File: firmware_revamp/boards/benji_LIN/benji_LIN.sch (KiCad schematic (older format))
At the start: 37 parts, among them J1 CONN_02X03, J2 Conn_01x11, J3 Conn_01x11, J4 CONN_01X03, J5 CONN_01x02, J6 CONN_01X03, SW1 SW_Push_SPST_NO, U1 MCP2561-E_SN, U2 ATMEGA16M1, U3 TLIN1021DRQ1, Y1 Crystal_SMD

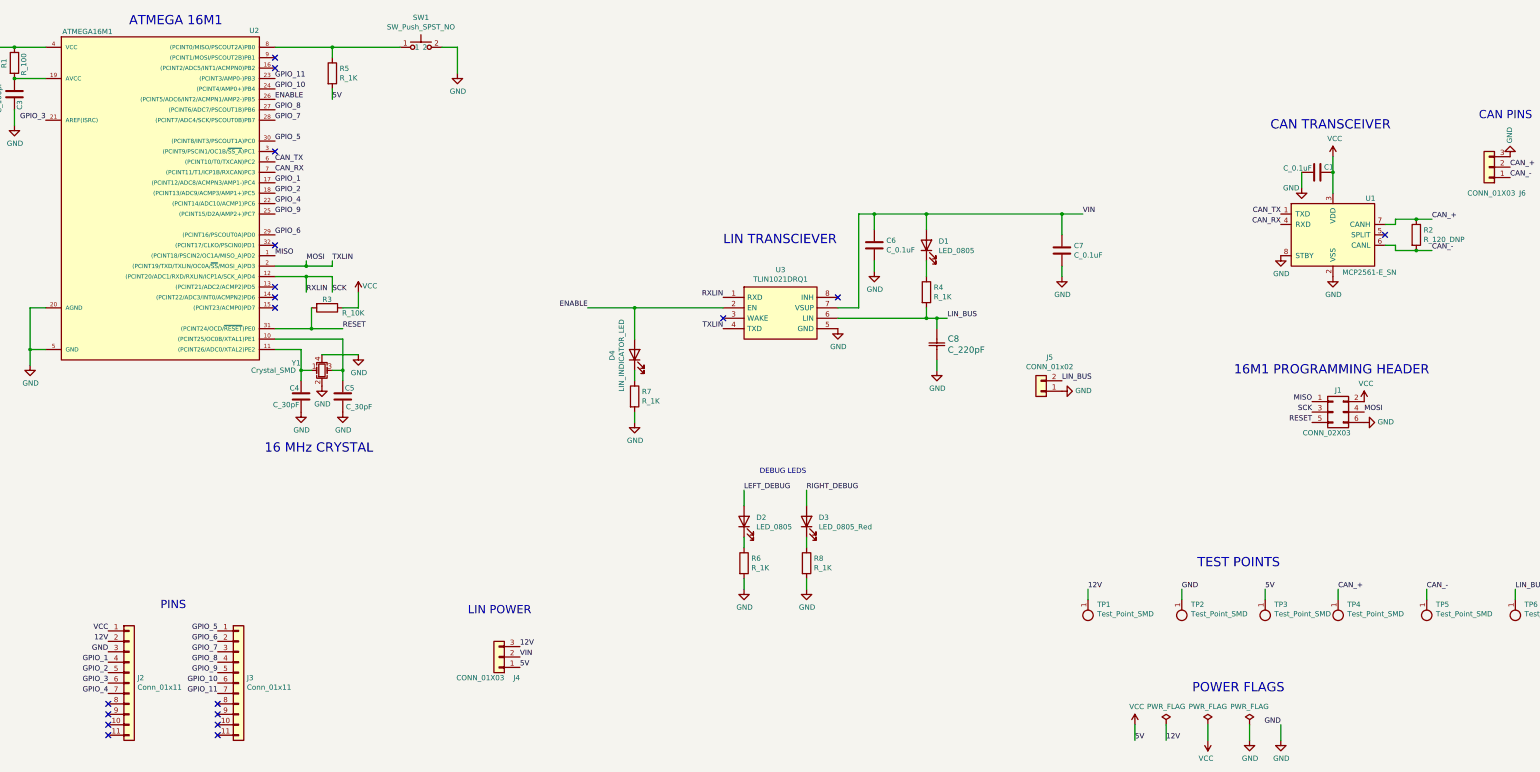
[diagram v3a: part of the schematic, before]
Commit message: Fixed vias, pins, rearranged debug lEDs
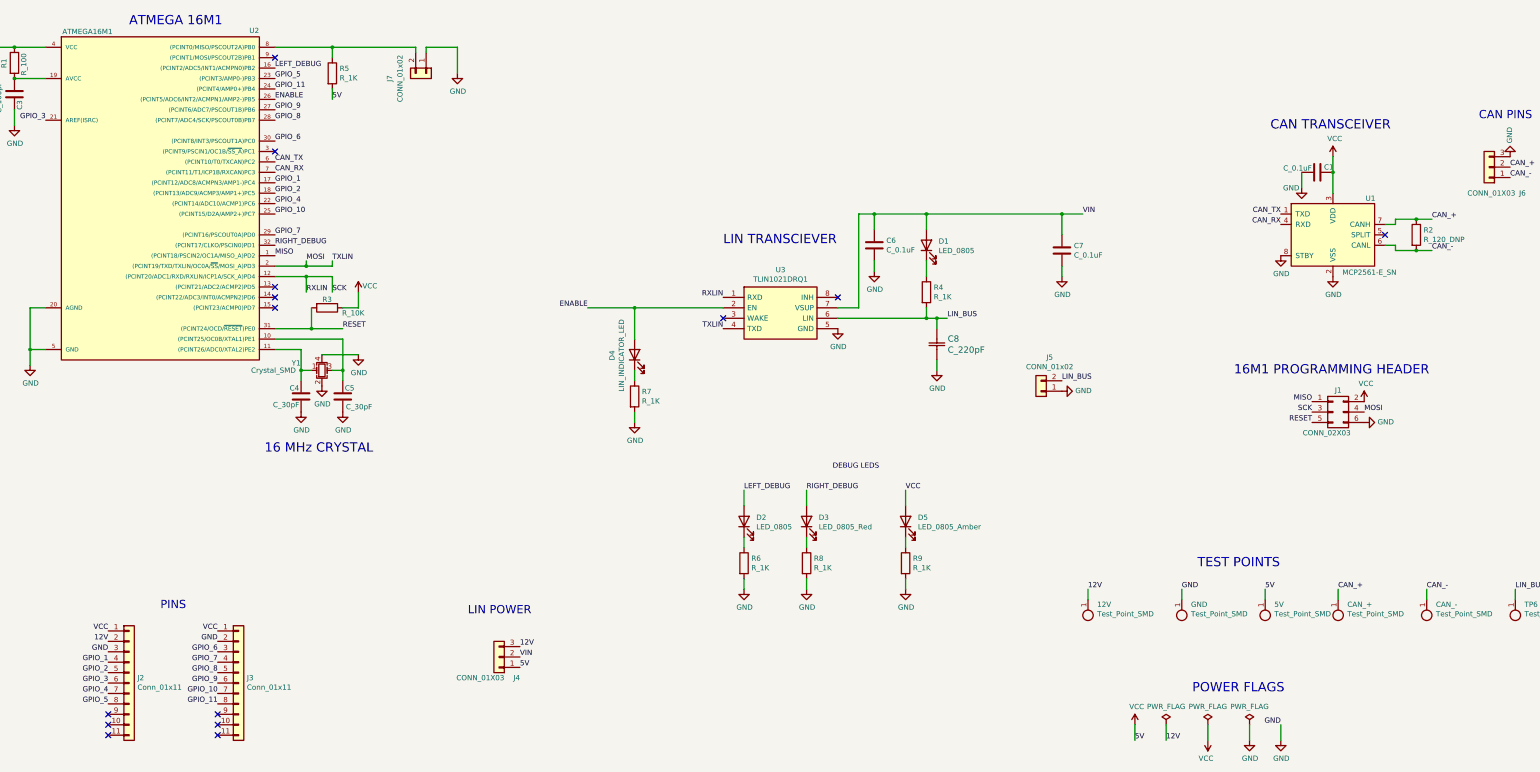
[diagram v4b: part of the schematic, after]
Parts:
- removed SW1: SW_Push_SPST_NO, footprints:SW_B3U-1000P_4.2x1.7mm, symbol formula:SW_Push_SPST_NO
- added D5: LED_0805_Amber, footprints:LED_0805_OEM, symbol formula:LED_0805_Amber
- added J7: CONN_01x02, Connector_PinHeader_2.54mm:PinHeader_1x02_P2.54mm_Vertical, symbol formula:CONN_01x02
- added R9: R_1K, footprints:R_0805_OEM, symbol formula:R_1K
- renumbered TP1 to 12V, TP3 to 5V, TP4 to CAN_+, TP5 to CAN_-, TP2 to GND
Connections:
- net GND: now also J3.2, J7.1 (Pin_1), R9.2
- net GPIO_10: now also J3.7, U2.25 ((PCINT15/D2A/AMP2+)PC7); no longer J3.6, U2.24 ((PCINT4/AMP0+)PB4)
- net GPIO_11: now also J3.8, U2.24 ((PCINT4/AMP0+)PB4); no longer J3.7, U2.23 ((PCINT3/AMP0-)PB3)
- net GPIO_5: now also J2.8, U2.23 ((PCINT3/AMP0-)PB3); no longer J3.1, U2.30 ((PCINT8/INT3/PSCOUT1A)PC0)
- net GPIO_6: now also J3.3, U2.30 ((PCINT8/INT3/PSCOUT1A)PC0); no longer J3.2, U2.29 ((PCINT16/PSCOUT0A)PD0)
- net GPIO_7: now also J3.4, U2.29 ((PCINT16/PSCOUT0A)PD0); no longer J3.3, U2.28 ((PCINT7/ADC4/SCK/PSCOUT0B)PB7)
- net GPIO_8: now also J3.5, U2.28 ((PCINT7/ADC4/SCK/PSCOUT0B)PB7); no longer J3.4, U2.27 ((PCINT6/ADC7/PSCOUT1B)PB6)
- net GPIO_9: now also J3.6, U2.27 ((PCINT6/ADC7/PSCOUT1B)PB6); no longer J3.5, U2.25 ((PCINT15/D2A/AMP2+)PC7)
- net LEFT_DEBUG: now also U2.16 ((PCINT2/ADC5/INT1/ACMPN0)PB2)
- net RIGHT_DEBUG: now also U2.32 ((PCINT17/CLKO/PSCIN0)PD1)
- net VCC: now also J3.1, D5.2 (A)
- net at R5.1, U2.8 ((PCINT0/MISO/PSCOUT2A)PB0): now also J7.2 (Pin_2)
- new net: D5.1 (K), R9.1
- no-connect marks 18 -> 14
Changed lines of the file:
@@
 Text Label 15550 6200 0    50   ~ 0
 LIN_BUS
-Text Notes 8300 5100 0    50   ~ 0
+Text Notes 9000 5050 0    50   ~ 0
 DEBUG LEDS
 $Comp
@@
 ENABLE
 NoConn ~ 3650 1100
-NoConn ~ 3650 1200
 NoConn ~ 3650 2000
-NoConn ~ 3650 2900
 Text Label 3650 3000 0    50   ~ 0
 MISO
@@
 Wire Wire Line
 	4200 1100 4200 1000
-Wire Wire Line
-	5400 1000 5250 1000
-$Comp
-L formula:SW_Push_SPST_NO SW1
-U 1 1 603700F1
-P 5050 1000
-F 0 "SW1" H 5050 1285 50  0000 C CNN
-F 1 "SW_Push_SPST_NO" H 5050 1194 50  0000 C CNN
-F 2 "footprints:SW_B3U-1000P_4.2x1.7mm" H 5050 1050 50  0001 C CNN
-F 3 "https://omronfs.omron.com/en_US/ecb/products/pdf/en-b3u.pdf" H 5050 1050 50  0001 C CNN
-F 4 "DK" H 5350 1350 50  0001 C CNN "MFN"
-F 5 "SW1020CT-ND" H 5250 1250 50  0001 C CNN "MPN"
-F 6 "https://www.digikey.com/product-detail/en/omron-electronics-inc-emc-div/B3U-1000P/SW1020CT-ND/1534357A" H 5450 1450 50  0001 C CNN "PurchasingLink"
-	1    5050 1000
-	1    0    0    -1
-$EndComp
 Wire Wire Line
 	3650 1000 4200 1000
@@
 $EndComp
 $Comp
-L formula:Test_Point_SMD TP1
+L formula:Test_Point_SMD 12V
 U 1 1 603FFDF1
 P 11450 6350
-F 0 "TP1" H 11362 6346 50  0000 R CNN
+F 0 "12V" H 11362 6346 50  0000 R CNN
 F 1 "Test_Point_SMD" H 11362 6437 50  0000 R CNN
 F 2 "footprints:Test_Point_SMD" H 11450 6200 50  0001 C CNN
@@
 $EndComp
 $Comp
-L formula:Test_Point_SMD TP2
+L formula:Test_Point_SMD GND
 U 1 1 60414A2B
 P 12350 6350
-F 0 "TP2" H 12262 6346 50  0000 R CNN
+F 0 "GND" H 12262 6346 50  0000 R CNN
 F 1 "Test_Point_SMD" H 12262 6437 50  0000 R CNN
 F 2 "footprints:Test_Point_SMD" H 12350 6200 50  0001 C CNN
@@
 $EndComp
 $Comp
-L formula:Test_Point_SMD TP3
+L formula:Test_Point_SMD 5V
 U 1 1 60414DEF
 P 13150 6350
-F 0 "TP3" H 13062 6346 50  0000 R CNN
+F 0 "5V" H 13062 6346 50  0000 R CNN
 F 1 "Test_Point_SMD" H 13062 6437 50  0000 R CNN
 F 2 "footprints:Test_Point_SMD" H 13150 6200 50  0001 C CNN
@@
 $EndComp
 $Comp
-L formula:Test_Point_SMD TP4
+L formula:Test_Point_SMD CAN_+
 U 1 1 60415519
 P 13850 6350
-F 0 "TP4" H 13762 6346 50  0000 R CNN
+F 0 "CAN_+" H 13762 6346 50  0000 R CNN
 F 1 "Test_Point_SMD" H 13762 6437 50  0000 R CNN
 F 2 "footprints:Test_Point_SMD" H 13850 6200 50  0001 C CNN
@@
 $EndComp
 $Comp
-L formula:Test_Point_SMD TP5
+L formula:Test_Point_SMD CAN_-
 U 1 1 604158E2
 P 14700 6350
-F 0 "TP5" H 14612 6346 50  0000 R CNN
+F 0 "CAN_-" H 14612 6346 50  0000 R CNN
 F 1 "Test_Point_SMD" H 14612 6437 50  0000 R CNN
 F 2 "footprints:Test_Point_SMD" H 14700 6200 50  0001 C CNN
@@
 Text Label 2050 6800 2    50   ~ 0
 GND
-NoConn ~ 3100 7300
 NoConn ~ 3100 7400
 NoConn ~ 3100 7500
@@
 NoConn ~ 2050 7500
 NoConn ~ 2050 7400
-NoConn ~ 2050 7300
 Connection ~ 4200 1000
 Wire Wire Line
 	5400 1000 5400 1250
-Wire Wire Line
-	4200 1000 4850 1000
 Text Label 6000 6850 0    50   ~ 0
 VIN
@@
 GPIO_4
 Text Label 3650 1300 0    50   ~ 0
+GPIO_5
+Text Label 3650 1400 0    50   ~ 0
 GPIO_11
-Text Label 3650 1400 0    50   ~ 0
-GPIO_10
 Text Label 3650 2300 0    50   ~ 0
 GPIO_1
@@
 GPIO_2
 Text Label 3650 1900 0    50   ~ 0
-GPIO_5
+GPIO_6
 Text Label 3650 2800 0    50   ~ 0
-GPIO_6
+GPIO_7
 Text Label 3650 1700 0    50   ~ 0
-GPIO_7
+GPIO_8
 Text Label 3650 1600 0    50   ~ 0
-GPIO_8
+GPIO_9
 Text Label 3650 2600 0    50   ~ 0
-GPIO_9
+GPIO_10
 $Comp
 L formula:Conn_01x11 J2
@@
 Text Label 2050 7200 2    50   ~ 0
 GPIO_4
+Text Label 2050 7300 2    50   ~ 0
+GPIO_5
+Text Label 3100 6800 2    50   ~ 0
+GPIO_6
+Text Label 3100 6900 2    50   ~ 0
+GPIO_7
+Text Label 3100 7000 2    50   ~ 0
+GPIO_8
+Text Label 3100 7100 2    50   ~ 0
+GPIO_9
+Text Label 3100 7200 2    50   ~ 0
+GPIO_10
+Text Label 3100 7300 2    50   ~ 0
+GPIO_11
+$Comp
+L formula:LED_0805_Amber D5
+U 1 1 606678A5
+P 9700 5550
+F 0 "D5" V 9739 5432 50  0000 R CNN
+F 1 "LED_0805_Amber" V 9648 5432 50  0000 R CNN
+F 2 "footprints:LED_0805_OEM" H 9600 5550 50  0001 C CNN
+F 3 "https://media.digikey.com/pdf/Data%20Sheets/Chicago%20Miniature%20Lamps%20PDFs/CMDA5_Series_Rev_Aug_2014.pdf" H 9700 5650 50  0001 C CNN
+F 4 "DK" H 9700 5550 60  0001 C CNN "MFN"
+F 5 "L71517CT-ND" H 9700 5550 60  0001 C CNN "MPN"
+F 6 "https://www.digikey.com/product-detail/en/visual-communications-company-vcc/CMDA5DY7D1S/L71517CT-ND/614867" H 10100 6050 60  0001 C CNN "PurchasingLink"
+	1    9700 5550
+	0    -1   -1   0
+$EndComp
+Text Label 9700 5250 0    50   ~ 0
+VCC
+Wire Wire Line
+	9700 5250 9700 5400
+$Comp
+L formula:R_1K R9
+U 1 1 6066FCA6
+P 9700 5950
+F 0 "R9" H 9770 5996 50  0000 L CNN
+F 1 "R_1K" H 9770 5905 50  0000 L CNN
+F 2 "footprints:R_0805_OEM" H 9630 5950 50  0001 C CNN
+F 3 "https://www.seielect.com/Catalog/SEI-rncp.pdf" H 9780 5950 50  0001 C CNN
+F 4 "DK" H 9700 5950 60  0001 C CNN "MFN"
+F 5 "RNCP0805FTD1K00CT-ND" H 9700 5950 60  0001 C CNN "MPN"
+F 6 "https://www.digikey.com/products/en?keywords=RNCP0805FTD1K00CT-ND" H 10180 6350 60  0001 C CNN "PurchasingLink"
+	1    9700 5950
+	1    0    0    -1
+$EndComp
+Wire Wire Line
+	9700 5800 9700 5700
+$Comp
+L power:GND #PWR024
+U 1 1 606730CC
+P 9700 6200
+F 0 "#PWR024" H 9700 5950 50  0001 C CNN
+F 1 "GND" H 9705 6027 50  0000 C CNN
+F 2 "" H 9700 6200 50  0001 C CNN
+F 3 "" H 9700 6200 50  0001 C CNN
+	1    9700 6200
+	1    0    0    -1
+$EndComp
+Wire Wire Line
+	9700 6200 9700 6100
+Text Label 3100 6700 2    50   ~ 0
+GND
 Text Label 3100 6600 2    50   ~ 0
-GPIO_5
-Text Label 3100 6700 2    50   ~ 0
-GPIO_6
-Text Label 3100 6800 2    50   ~ 0
-GPIO_7
-Text Label 3100 6900 2    50   ~ 0
-GPIO_8
-Text Label 3100 7000 2    50   ~ 0
-GPIO_9
-Text Label 3100 7100 2    50   ~ 0
-GPIO_10
-Text Label 3100 7200 2    50   ~ 0
-GPIO_11
+VCC
+$Comp
+L formula:CONN_01x02 J7
+U 1 1 60655BBB
+P 5100 1250
+F 0 "J7" H 5150 900 50  0000 C CNN
+F 1 "CONN_01x02" H 5150 1000 50  0000 C CNN
+F 2 "Connector_PinHeader_2.54mm:PinHeader_1x02_P2.54mm_Vertical" H 5000 1250 50  0001 C CNN
+F 3 "https://katalog.we-online.de/em/datasheet/6130xx11121.pdf" H 5100 1350 50  0001 C CNN
+F 4 "DK" H 5200 1450 50  0001 C CNN "MFN"
+F 5 "732-5315-ND" H 5300 1550 50  0001 C CNN "MPN"
+	1    5100 1250
+	0    1    1    0
+$EndComp
+Wire Wire Line
+	5000 1000 5000 1050
+Wire Wire Line
+	4200 1000 5000 1000
+Wire Wire Line
+	5100 1000 5100 1050
+Wire Wire Line
+	5100 1000 5400 1000
+Text Label 3650 2900 0    50   ~ 0
+RIGHT_DEBUG
+Text Label 3650 1200 0    50   ~ 0
+LEFT_DEBUG
 $EndSCHEMATC

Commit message: Rearranged mostly visual errors, removed diode
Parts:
- removed D1: LED_0805, footprints:LED_0805_OEM, symbol formula:LED_0805
- removed GND: Test_Point_SMD, footprints:Test_Point_SMD, symbol formula:Test_Point_SMD
- renumbered 12V to 12V1, 5V to 5V1, CAN_+ to CAN_+1, CAN_- to CAN_-1
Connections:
- net ENABLE: now also U2.9 ((PCINT1/MOSI/PSCOUT2B)PB1); no longer U2.26 ((PCINT5/ADC6/INT2/ACMPN1/AMP2-)PB5)
- net GND: now also J3.1; no longer J3.2
- net LEFT_DEBUG: now also U2.13 ((PCINT21/ADC2/ACMP2)PD5); no longer U2.16 ((PCINT2/ADC5/INT1/ACMPN0)PB2)
- net RIGHT_DEBUG: now also U2.14 ((PCINT22/ADC3/INT0/ACMPN2)PD6); no longer U2.32 ((PCINT17/CLKO/PSCIN0)PD1)
- net VCC: no longer J3.1
- net VIN: now also R4.1
- net PD7: now reaches U2.15 ((PCINT23/ACMP0)PD7)
- net PD7: now also J2.4
- net PB4: now reaches J2.9
- net PB4: now also U2.24 ((PCINT4/AMP0+)PB4)
- net PC5: now reaches J3.9
- net PC5: now also U2.18 ((PCINT13/ADC9/ACMP3/AMP1+)PC5)
- net GPIO_1 renamed PC4
- net PC4: now also J2.6; no longer J2.4
- net GPIO_10 renamed PC7
- net GPIO_11 renamed PD1
- net PD1: now also U2.32 ((PCINT17/CLKO/PSCIN0)PD1); no longer U2.24 ((PCINT4/AMP0+)PB4)
- net GPIO_2 renamed PB2
- net PB2: now also U2.16 ((PCINT2/ADC5/INT1/ACMPN0)PB2); no longer U2.18 ((PCINT13/ADC9/ACMP3/AMP1+)PC5)
- net GPIO_3: no longer names the net of U2.21 (AREF(ISRC))
- net GPIO_3: no longer J2.6
- net GPIO_4 renamed PC6
- net GPIO_5 renamed PB3
- net GPIO_6 renamed PC0
- net PC0: now also J3.2; no longer J3.3
- net GPIO_7 renamed PB7
- net PB7: now also U2.28 ((PCINT7/ADC4/SCK/PSCOUT0B)PB7); no longer U2.29 ((PCINT16/PSCOUT0A)PD0)
- net GPIO_8 renamed PB6
- net PB6: now also U2.27 ((PCINT6/ADC7/PSCOUT1B)PB6); no longer U2.28 ((PCINT7/ADC4/SCK/PSCOUT0B)PB7)
- net GPIO_9 renamed PB5
- net PB5: now also U2.26 ((PCINT5/ADC6/INT2/ACMPN1/AMP2-)PB5); no longer U2.27 ((PCINT6/ADC7/PSCOUT1B)PB6)
- new net PD0: J3.3, U2.29 ((PCINT16/PSCOUT0A)PD0)
- no-connect marks 14 -> 9
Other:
- moved on the sheet: R3, R4

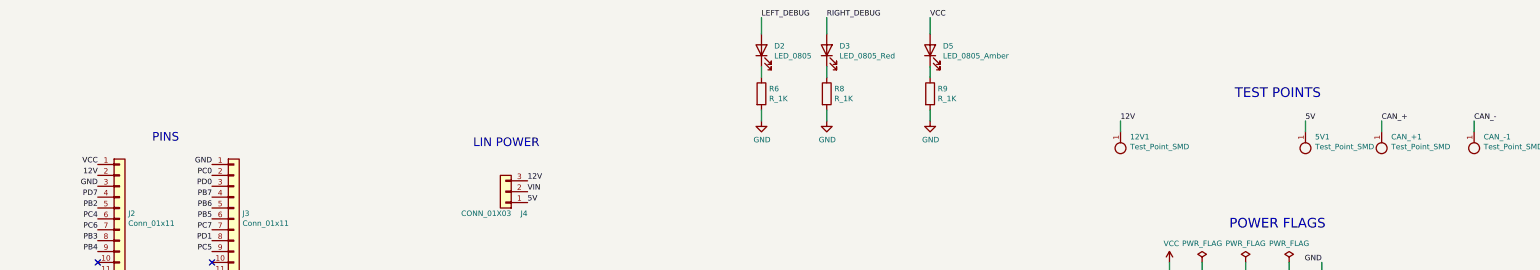
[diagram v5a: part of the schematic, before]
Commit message: Add labels to headers
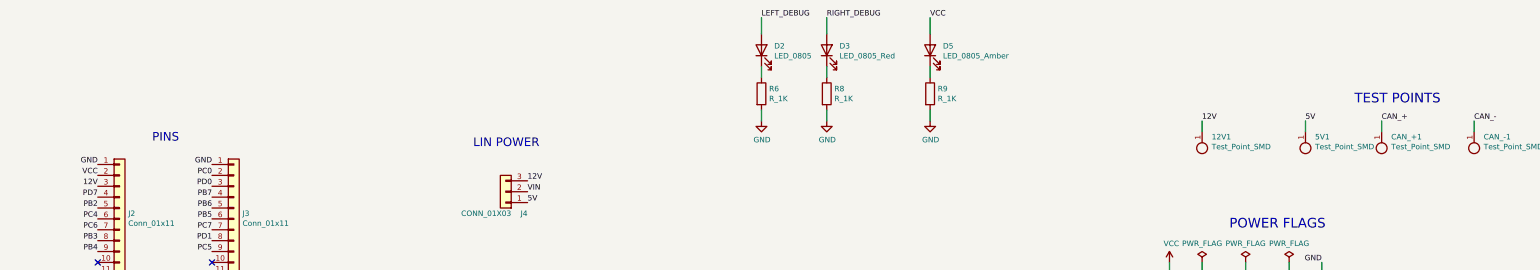
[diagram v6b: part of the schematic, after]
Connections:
- net 12V: now also J2.3; no longer J2.2
- net GND: now also J2.1; no longer J2.3
- net VCC: now also J2.2; no longer J2.1
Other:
- moved on the sheet: 12V1
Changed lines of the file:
@@
 Wire Wire Line
 	15550 6300 15550 6200
-Text Notes 12500 6000 0    89   ~ 0
+Text Notes 13600 6050 0    89   ~ 0
 TEST POINTS
 Wire Wire Line
-	11450 6200 11450 6300
-Text Label 11450 6200 0    50   ~ 0
+	12200 6200 12200 6300
+Text Label 12200 6200 0    50   ~ 0
 12V
 Text Label 7950 3400 2    50   ~ 0
@@
 L formula:Test_Point_SMD 12V1
 U 1 1 603FFDF1
-P 11450 6350
-F 0 "12V1" H 11362 6346 50  0000 R CNN
-F 1 "Test_Point_SMD" H 11362 6437 50  0000 R CNN
-F 2 "footprints:Test_Point_SMD" H 11450 6200 50  0001 C CNN
-F 3 "" H 11450 6350 50  0001 C CNN
-	1    11450 6350
+P 12200 6350
+F 0 "12V1" H 12112 6346 50  0000 R CNN
+F 1 "Test_Point_SMD" H 12112 6437 50  0000 R CNN
+F 2 "footprints:Test_Point_SMD" H 12200 6200 50  0001 C CNN
+F 3 "" H 12200 6350 50  0001 C CNN
+	1    12200 6350
 	-1   0    0    1
 $EndComp
@@
 ENABLE
 Text Label 2050 6600 2    50   ~ 0
-VCC
-Text Label 2050 6800 2    50   ~ 0
 GND
 NoConn ~ 3100 7500
@@
 	0    -1   -1   0
 $EndComp
-Text Label 2050 6700 2    50   ~ 0
-12V
 Wire Wire Line
 	1150 1600 1150 1750
@@
 Text Label 3100 6900 2    50   ~ 0
 PB7
+Text Label 2050 6800 2    50   ~ 0
+12V
+Text Label 2050 6700 2    50   ~ 0
+VCC
 $EndSCHEMATC

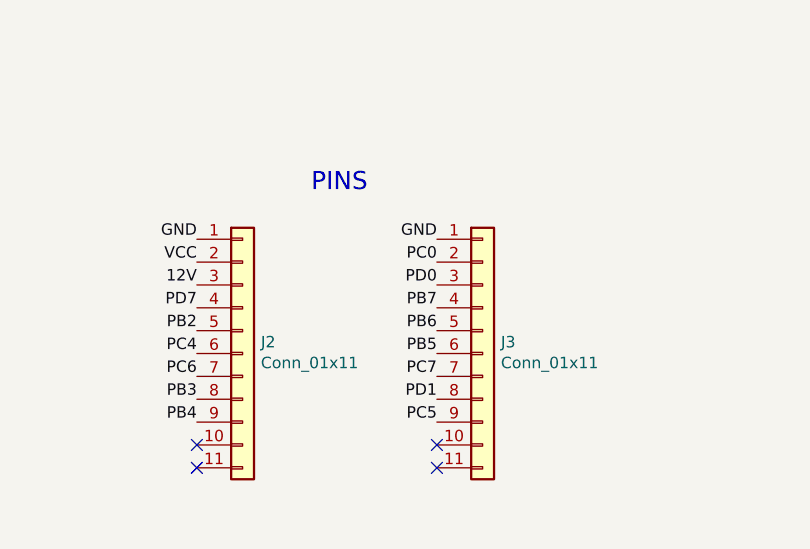
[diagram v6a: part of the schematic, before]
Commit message: Used correct headers, renamed pins where necessary
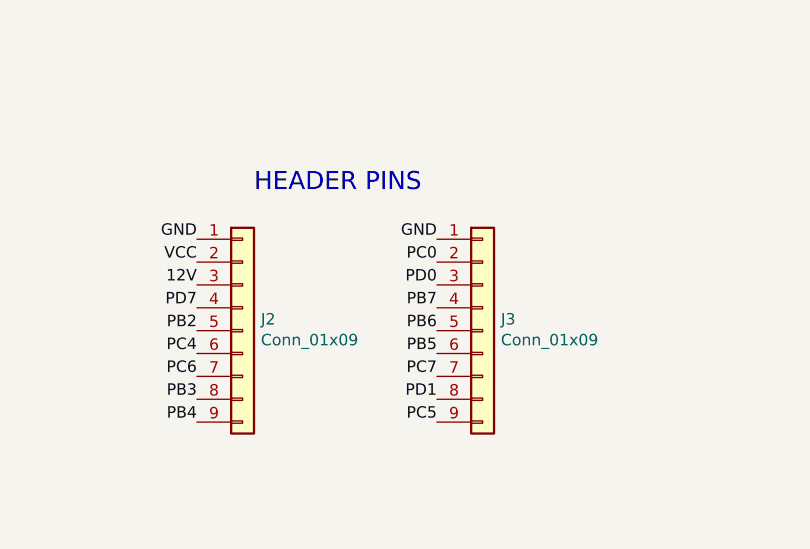
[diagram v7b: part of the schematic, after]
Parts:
- removed J2, J3: Conn_01x11, footprints:PinHeader_1x11_P2.54mm_Vertical, symbol formula:Conn_01x11
- added J2, J3: Conn_01x09, footprints:PinHeader_1x9_P2.54mm_Vertical, symbol formula:Conn_01x09
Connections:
- net 12V: now also J2.3
- net GND: now also J2.1, J3.1
- net PB2: now also J2.5
- net PB3: now also J2.8
- net PB4: now also J2.9
- net PB5: now also J3.6
- net PB6: now also J3.5
- net PB7: now also J3.4
- net PC0: now also J3.2
- net PC4: now also J2.6
- net PC5: now also J3.9
- net PC6: now also J2.7
- net PC7: now also J3.7
- net PD0: now also J3.3
- net PD1: now also J3.8
- net PD7: now also J2.4
- net VCC: now also J2.2
- no-connect marks 9 -> 5
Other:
- note added: "HEADER PINS"
- note removed: "PINS"
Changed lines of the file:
@@
 Text Label 8150 5250 0    50   ~ 0
 LEFT_DEBUG
-Text Notes 2550 6400 0    79   ~ 0
-PINS
+Text Notes 2300 6400 0    79   ~ 0
+HEADER PINS
 Text Notes 5500 6450 0    79   ~ 0
 LIN POWER
@@
 Text Label 2050 6600 2    50   ~ 0
 GND
-NoConn ~ 3100 7500
-NoConn ~ 3100 7600
-NoConn ~ 2050 7600
-NoConn ~ 2050 7500
 Connection ~ 4200 1000
 Wire Wire Line
@@
 Text Label 3650 2600 0    50   ~ 0
 PC7
-$Comp
-L formula:Conn_01x11 J2
-U 1 1 603F6805
-P 2250 7150
-F 0 "J2" H 2330 7250 50  0000 L CNN
-F 1 "Conn_01x11" H 2330 7159 50  0000 L CNN
-F 2 "footprints:PinHeader_1x11_P2.54mm_Vertical" H 2150 7850 50  0001 C CNN
-F 3 "" H 2250 7150 50  0001 C CNN
-	1    2250 7150
-	1    0    0    -1
-$EndComp
 Text Label 2050 6900 2    50   ~ 0
 PD7
@@
 Text Label 3100 6700 2    50   ~ 0
 PC0
-$Comp
-L formula:Conn_01x11 J3
-U 1 1 6040C0B1
-P 3300 7150
-F 0 "J3" H 3380 7250 50  0000 L CNN
-F 1 "Conn_01x11" H 3380 7159 50  0000 L CNN
-F 2 "footprints:PinHeader_1x11_P2.54mm_Vertical" H 3200 7850 50  0001 C CNN
-F 3 "" H 3300 7150 50  0001 C CNN
-	1    3300 7150
-	1    0    0    -1
-$EndComp
 Text Label 3100 6900 2    50   ~ 0
 PB7
@@
 Text Label 2050 6700 2    50   ~ 0
 VCC
+$Comp
+L formula:Conn_01x09 J2
+U 1 1 6064A828
+P 2250 7000
+F 0 "J2" H 2330 7050 50  0000 L CNN
+F 1 "Conn_01x09" H 2330 6959 50  0000 L CNN
+F 2 "footprints:PinHeader_1x9_P2.54mm_Vertical" H 2250 6450 50  0001 C CNN
+F 3 "" H 2250 6500 50  0001 C CNN
+	1    2250 7000
+	1    0    0    -1
+$EndComp
+$Comp
+L formula:Conn_01x09 J3
+U 1 1 60655A24
+P 3300 7000
+F 0 "J3" H 3380 7050 50  0000 L CNN
+F 1 "Conn_01x09" H 3380 6959 50  0000 L CNN
+F 2 "footprints:PinHeader_1x9_P2.54mm_Vertical" H 3300 6450 50  0001 C CNN
+F 3 "" H 3300 6500 50  0001 C CNN
+	1    3300 7000
+	1    0    0    -1
+$EndComp
 $EndSCHEMATC
